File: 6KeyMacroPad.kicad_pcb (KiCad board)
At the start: 2 copper layers, 39 parts, among them SW1 SW_Push, U1 ATmega32U4-A, Y1 16 MHz

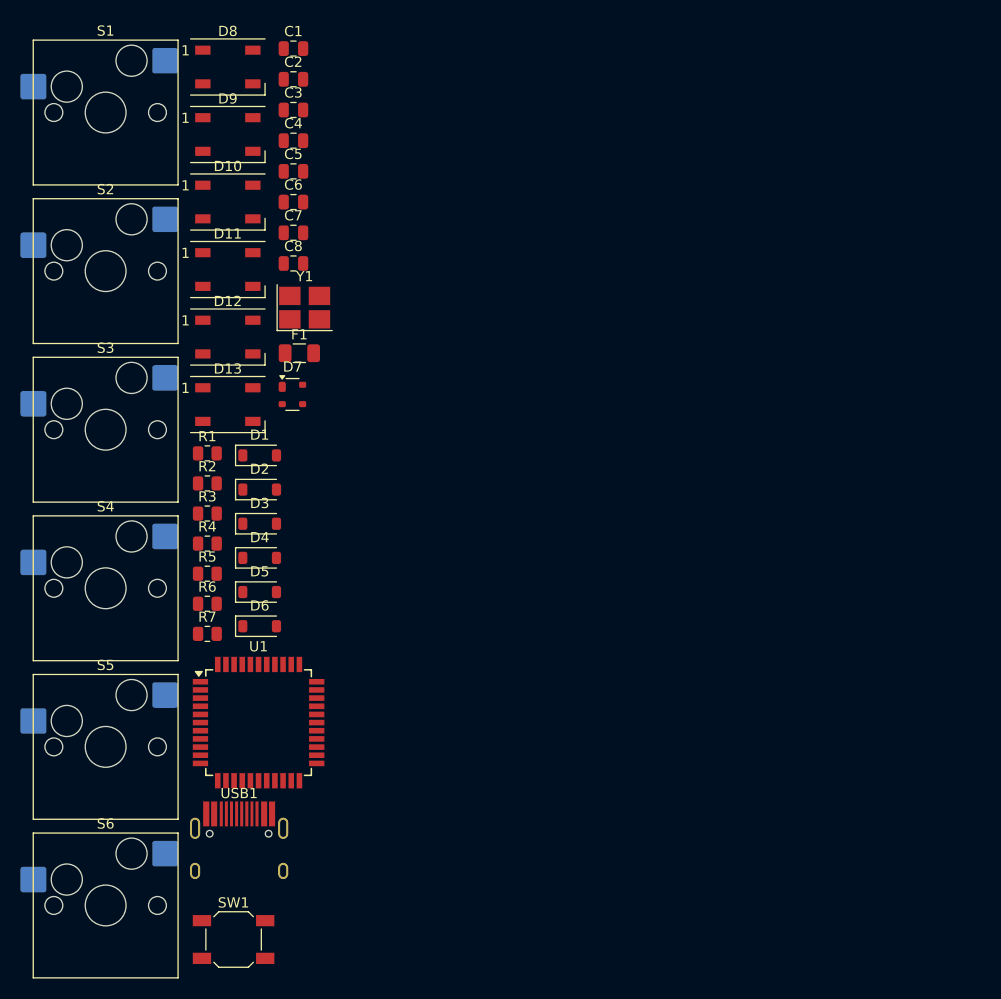
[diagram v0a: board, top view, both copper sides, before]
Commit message: board layout updates
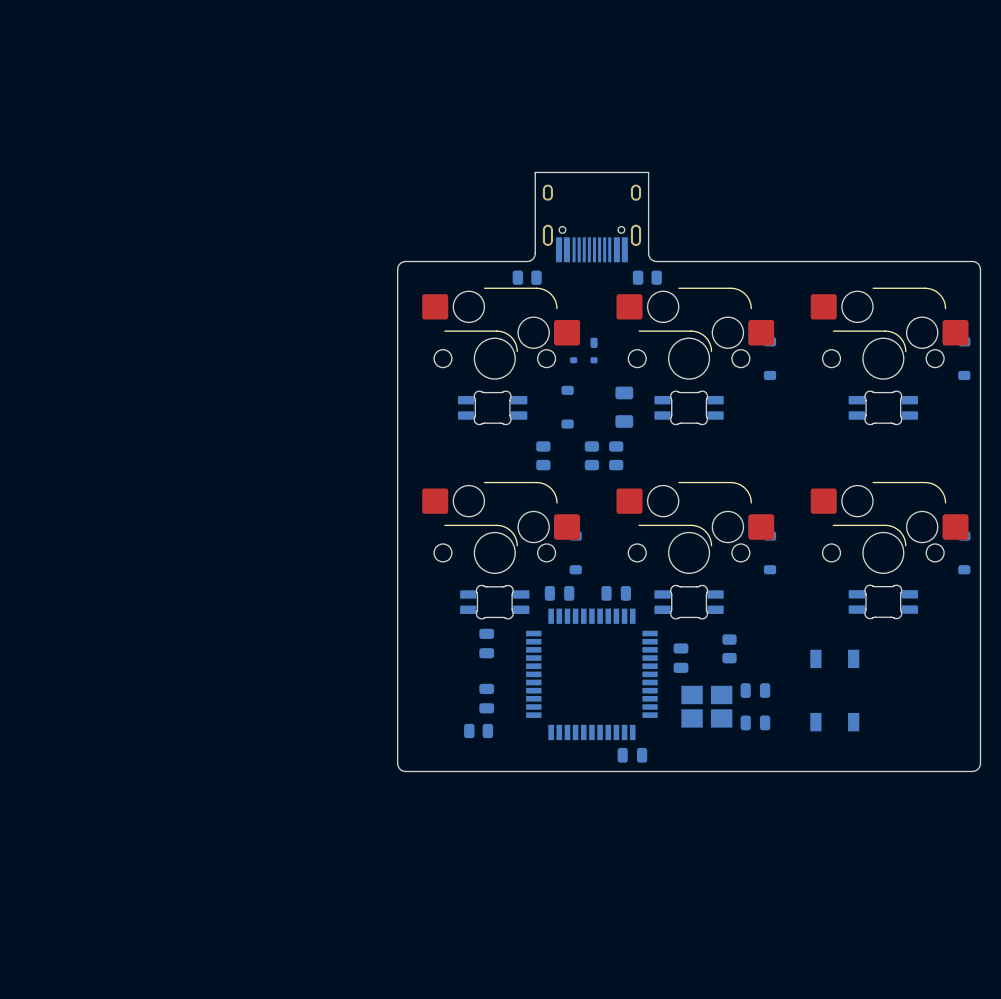
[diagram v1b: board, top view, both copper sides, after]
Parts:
- C1, C2, C3, C4, C5, C6, C7, C8, D1, D2, D3, D4, D5, D6, D7, F1, R1, R2, R3, R4, R5, R6, R7, S1, S2, S3, S4, S5, S6, SW1, U1, USB1, Y1: moved to B.Cu
- D10, D11, D12, D13, D8, D9: value WS2812B -> SK6812MINI; footprint LED_SMD:LED_WS2812B_PLCC4_5.0x5.0mm_P3.2mm -> kicad-keyboard-parts:MX_SK6812MINI-E
- moved S5 85.2 mm to (189.7, 80.2), turned to 180 degrees
- moved S6 83.7 mm to (189.7, 99.2), turned to 180 degrees
- moved C1 80.1 mm to (177.2, 115.9)
- moved USB1 79.6 mm to (161.1, 61.3)
- moved C2 75.1 mm to (177.2, 112.7)
- moved D5 72.8 mm to (197.6, 80.2), turned to 90 degrees
- moved D11 69.9 mm to (189.7, 98.9)
- moved D6 69.5 mm to (197.6, 99.2), turned to 90 degrees
- moved C4 68.8 mm to (165.1, 119.1)
- moved D10 66.0 mm to (189.7, 79.9)
- moved SW1 63.8 mm to (184.9, 112.7), turned to 90 degrees
- moved C6 58.7 mm to (169.9, 109.5), turned to -90 degrees
- moved S3 57.6 mm to (170.7, 80.2), turned to 180 degrees
- moved S4 57.3 mm to (170.7, 99.2), turned to 180 degrees
- moved C3 57.0 mm to (163.5, 103.2), turned to 180 degrees
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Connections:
- D10 pad 1: +5V -> Net-(D10-DOUT)
- D10 pad 2: Net-(D10-DOUT) -> GND
- D10 pad 3: GND -> Net-(D10-DIN)
- D10 pad 4: Net-(D10-DIN) -> +5V
- D11 pad 1: +5V -> Net-(D11-DOUT)
- D11 pad 2: Net-(D11-DOUT) -> GND
- D11 pad 3: GND -> Net-(D10-DOUT)
- D11 pad 4: Net-(D10-DOUT) -> +5V
- D12 pad 1: +5V -> Net-(D12-DOUT)
- D12 pad 2: Net-(D12-DOUT) -> GND
- D12 pad 3: GND -> Net-(D11-DOUT)
- D12 pad 4: Net-(D11-DOUT) -> +5V
- D13 pad 1: +5V -> unconnected-(D13-DOUT-Pad1)
- D13 pad 2: unconnected-(D13-DOUT-Pad2) -> GND
- D13 pad 3: GND -> Net-(D12-DOUT)
- D13 pad 4: Net-(D12-DOUT) -> +5V
- D8 pad 1: +5V -> Net-(D8-DOUT)
- D8 pad 2: Net-(D8-DOUT) -> GND
- D8 pad 3: GND -> LEDs
- D8 pad 4: LEDs -> +5V
- D9 pad 1: +5V -> Net-(D10-DIN)
- D9 pad 2: Net-(D10-DIN) -> GND
- D9 pad 3: GND -> Net-(D8-DOUT)
- D9 pad 4: Net-(D8-DOUT) -> +5V
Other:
- board outline added: 57.1 x 58.7 mm

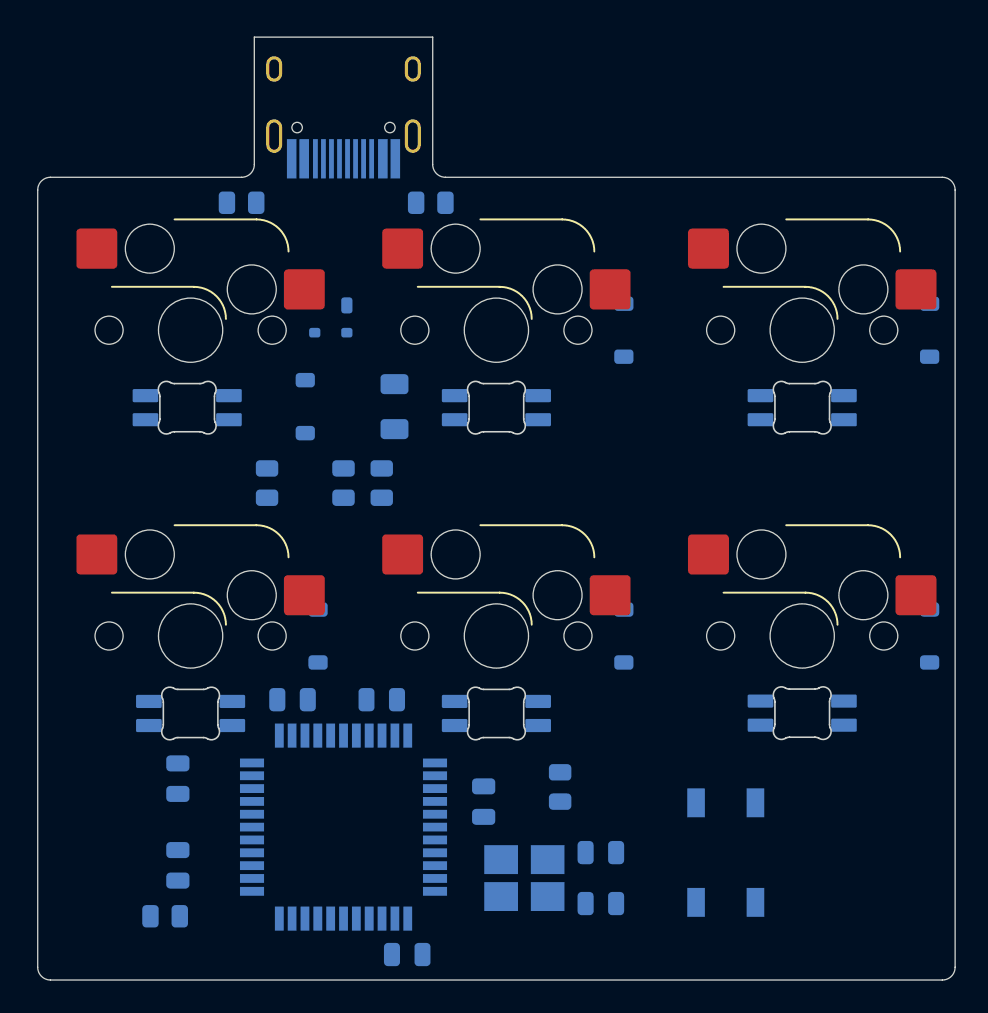
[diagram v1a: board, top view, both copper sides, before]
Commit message: footprint edits, routing updates
drc checked
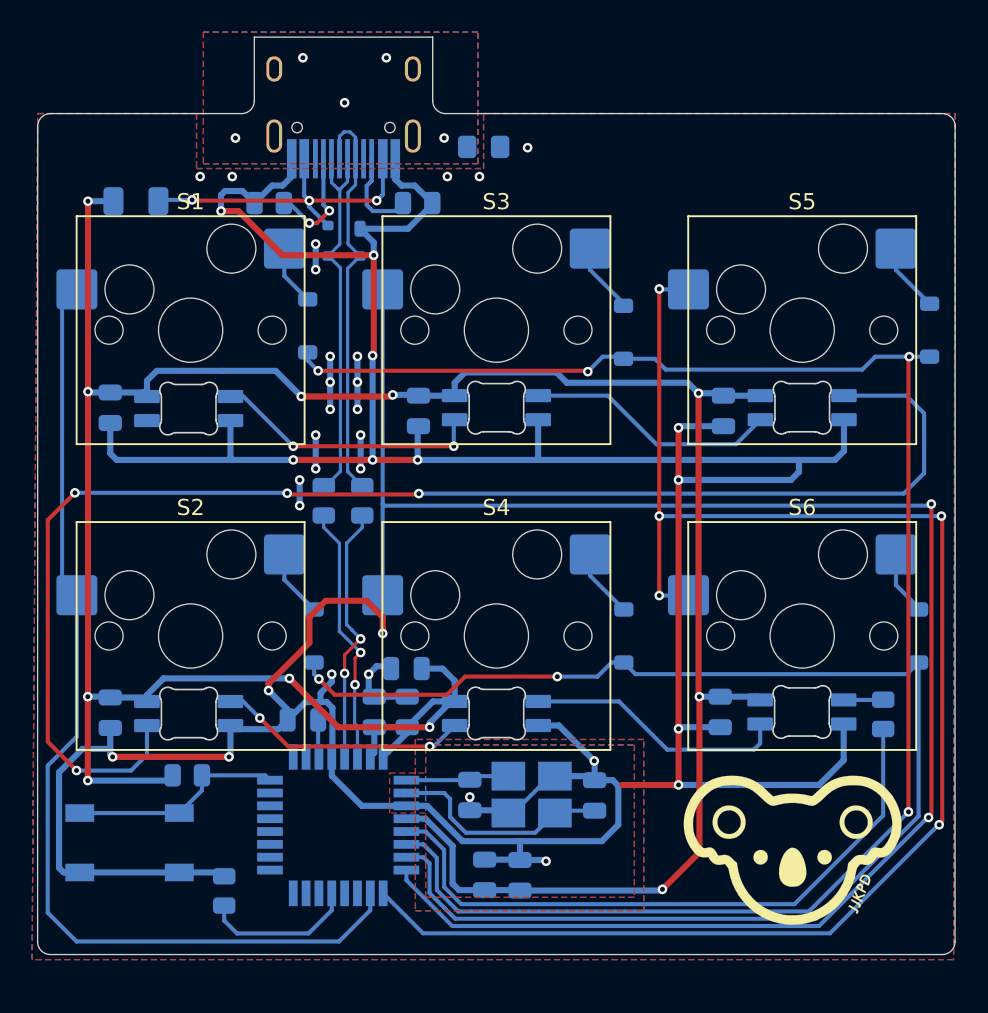
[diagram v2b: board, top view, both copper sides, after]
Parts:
- removed U1: ATmega32U4-A, Package_QFP:TQFP-44_10x10mm_P0.8mm
- added C10: 100 nF, Capacitor_SMD:C_0805_2012Metric, B.Cu at (184.8, 85.2)
- added C11: 100 nF, Capacitor_SMD:C_0805_2012Metric, B.Cu at (184.6, 104.0)
- added C12: 100 nF, Capacitor_SMD:C_0805_2012Metric, B.Cu at (165.1, 101.2)
- added C13: 100 nF, Capacitor_SMD:C_0805_2012Metric, B.Cu at (146.6, 104.0)
- added C9: 100 nF, Capacitor_SMD:C_0805_2012Metric, B.Cu at (165.8, 85.2)
- added FB1: 60@100MHz, Inductor_SMD:L_0805_2012Metric_Pad1.15x1.40mm_HandSolder, B.Cu at (169.9, 68.8)
- added Ref**: Val**, 6KeyMacroPad:jjkpdlogo, F.Cu at (191.6, 115.2)
- added U2: ATmega32U2-A, Package_QFP:TQFP-32_7x7mm_P0.8mm, B.Cu at (160.8, 111.0)
- C7: value 0.1 uF -> 10 uF
- C8: value 10 uF -> 100 nF
- D10, D11, D12, D13, D8, D9: value SK6812MINI -> SK6812MINI-E
- S1, S2, S3, S4, S5, S6: moved to F.Cu
- moved R7 41.0 mm to (194.8, 104.1)
- moved D11 38.2 mm to (151.5, 99.0)
- moved D13 38.1 mm to (189.7, 98.9)
- moved SW1 37.1 mm to (147.8, 112.1), turned to 0 degrees
- moved R3 23.2 mm to (151.4, 107.9), turned to 0 degrees
- moved C8 21.4 mm to (146.6, 85.0), turned to 90 degrees
- moved C7 21.3 mm to (172.1, 114.1)
- moved F1 20.6 mm to (148.2, 72.1), turned to 180 degrees
- moved C4 15.1 mm to (165.1, 104.0), turned to 90 degrees
- moved C5 12.9 mm to (163.1, 104.0), turned to 90 degrees
- moved C1 10.6 mm to (169.0, 109.1), turned to -90 degrees
- moved Y1 5.22 mm to (172.8, 109.1), turned to 0 degrees
- moved C3 5.07 mm to (158.6, 104.5)
- moved D1 5.03 mm to (158.9, 79.9)
- moved D7 4.85 mm to (161.2, 74.6)
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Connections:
- C8 pad 1: +5V -> GND
- C8 pad 2: GND -> +5V
- D10 pad 1: Net-(D10-DOUT) -> +5V
- D10 pad 2: GND -> Net-(D10-DOUT)
- D10 pad 3: Net-(D10-DIN) -> GND
- D10 pad 4: +5V -> Net-(D10-DIN)
- D11 pad 1: Net-(D11-DOUT) -> +5V
- D11 pad 2: GND -> Net-(D10-DIN)
- D11 pad 3: Net-(D10-DOUT) -> GND
- D11 pad 4: +5V -> Net-(D11-DIN)
- D12 pad 1: Net-(D12-DOUT) -> +5V
- D12 pad 2: GND -> Net-(D11-DIN)
- D12 pad 3: Net-(D11-DOUT) -> GND
- D12 pad 4: +5V -> Net-(D12-DIN)
- D13 pad 1: unconnected-(D13-DOUT-Pad1) -> +5V
- D13 pad 2: GND -> Net-(D12-DIN)
- D13 pad 3: Net-(D12-DOUT) -> GND
- D13 pad 4: +5V -> D1
- D8 pad 1: Net-(D8-DOUT) -> +5V
- D8 pad 2: GND -> unconnected-(D8-DOUT-Pad2)
- D8 pad 3: LEDs -> GND
- D8 pad 4: +5V -> Net-(D8-DIN)
- D9 pad 1: Net-(D10-DIN) -> +5V
- D9 pad 2: GND -> Net-(D8-DIN)
- D9 pad 3: Net-(D8-DOUT) -> GND
- D9 pad 4: +5V -> Net-(D10-DOUT)
- R7 pad 1: LEDs -> D1
- USB1 pad 13: GND -> Earth
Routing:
- net GND: track 0.00 -> 275.4 mm, vias 0 -> 38
- net +5V: track 0.00 -> 183.5 mm, vias 0 -> 11
- net Column 1: track 0.00 -> 110.1 mm, vias 0 -> 2
- net Row 0: track 0.00 -> 105.7 mm, vias 0 -> 4
- net Column 2: track 0.00 -> 98.1 mm, vias 0 -> 5
- net Net-(D10-DIN): track 0.00 -> 88.0 mm, vias 0 -> 4
- net Row 1: track 0.00 -> 87.1 mm, vias 0 -> 2
- net Column 0: track 0.00 -> 63.0 mm
- net Net-(U2-PC2): track 0.00 -> 40.6 mm
- net D+: track 0.00 -> 25.6 mm
- net D-: track 0.00 -> 23.9 mm
- net VCC: track 0.00 -> 21.2 mm, vias 0 -> 3
- net Net-(D8-DIN): track 0.00 -> 16.9 mm, vias 0 -> 2
- net Net-(U2-D+): track 0.00 -> 16.5 mm, vias 0 -> 2
- net Net-(U2-D-): track 0.00 -> 16.5 mm, vias 0 -> 2
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- added copper zone on B.Cu, net Earth
- added copper zone on F.Cu, net Earth
- added copper zone on B.Cu, net GND
- added copper zone on F.Cu, net GND
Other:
- board size 57.1 x 58.7 mm -> 57.2 x 57.1 mm

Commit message: manufacturing files changed
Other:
- board text added: "V1.0"
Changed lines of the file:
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@@
 		(allow_soldermask_bridges_in_footprints no)
 		(pcbplotparams
-			(layerselection 0x00010fc_ffffffff)
+			(layerselection 0x00010f0_ffffffff)
 			(plot_on_all_layers_selection 0x0000000_00000000)
 			(disableapertmacros no)
 			(usegerberextensions no)
-			(usegerberattributes yes)
-			(usegerberadvancedattributes yes)
-			(creategerberjobfile yes)
+			(usegerberattributes no)
+			(usegerberadvancedattributes no)
+			(creategerberjobfile no)
 			(dashed_line_dash_ratio 12.000000)
 			(dashed_line_gap_ratio 3.000000)
@@
 			(outputformat 1)
 			(mirror no)
-			(drillshape 1)
+			(drillshape 0)
 			(scaleselection 1)
-			(outputdirectory "")
+			(outputdirectory "Manufacturing/")
 		)
 	)
@@
 		(fp_arc
 			(start 1.699999 4.377156)
-			(mid 1.712525 4.26593)
+			(mid 1.712526 4.26593)
 			(end 1.749484 4.160279)
 			(stroke
@@
 		(fp_arc
 			(start 1.749484 5.999719)
-			(mid 1.712517 5.89407)
+			(mid 1.712511 5.89407)
 			(end 1.699999 5.782841)
 			(stroke
@@
 		(fp_arc
 			(start 1.699999 4.377156)
-			(mid 1.712525 4.26593)
+			(mid 1.712526 4.26593)
 			(end 1.749484 4.160279)
 			(stroke
@@
 		(fp_arc
 			(start 1.749484 5.999719)
-			(mid 1.712517 5.89407)
+			(mid 1.712511 5.89407)
 			(end 1.699999 5.782841)
 			(stroke
@@
 		(fp_arc
 			(start 1.699999 4.377156)
-			(mid 1.712525 4.26593)
+			(mid 1.712526 4.26593)
 			(end 1.749484 4.160279)
 			(stroke
@@
 		(fp_arc
 			(start 1.749484 5.999719)
-			(mid 1.712517 5.89407)
+			(mid 1.712511 5.89407)
 			(end 1.699999 5.782841)
 			(stroke
@@
 		(fp_arc
 			(start 1.699999 4.377156)
-			(mid 1.712525 4.26593)
+			(mid 1.712526 4.26593)
 			(end 1.749484 4.160279)
 			(stroke
@@
 		(fp_arc
 			(start 1.749484 5.999719)
-			(mid 1.712517 5.89407)
+			(mid 1.712511 5.89407)
 			(end 1.699999 5.782841)
 			(stroke
@@
 		(fp_arc
 			(start 1.699999 4.377156)
-			(mid 1.712525 4.26593)
+			(mid 1.712526 4.26593)
 			(end 1.749484 4.160279)
 			(stroke
@@
 		(fp_arc
 			(start 1.749484 5.999719)
-			(mid 1.712517 5.89407)
+			(mid 1.712511 5.89407)
 			(end 1.699999 5.782841)
 			(stroke
@@
 		(fp_arc
 			(start 1.699999 4.377156)
-			(mid 1.712525 4.26593)
+			(mid 1.712526 4.26593)
 			(end 1.749484 4.160279)
 			(stroke
@@
 		(fp_arc
 			(start 1.749484 5.999719)
-			(mid 1.712517 5.89407)
+			(mid 1.712511 5.89407)
 			(end 1.699999 5.782841)
 			(stroke
@@
 		(layer "Edge.Cuts")
 	)
+	(gr_text "V1.0"
+		(at 195.6 118.6 0)
+		(layer "F.SilkS")
+		(effects
+			(font
+				(size 0.762 0.762)
+				(thickness 0.1905)
+				(bold yes)
+			)
+			(justify left bottom)
+		)
+	)
 	(segment
